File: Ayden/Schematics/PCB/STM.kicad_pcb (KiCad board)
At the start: 2 copper layers, 104.1 x 88.9 mm, 8 parts, among them J1 Screw_Terminal_01x12, U1 NUCLEO-F103RB, U2 NRF24L01_Breakout

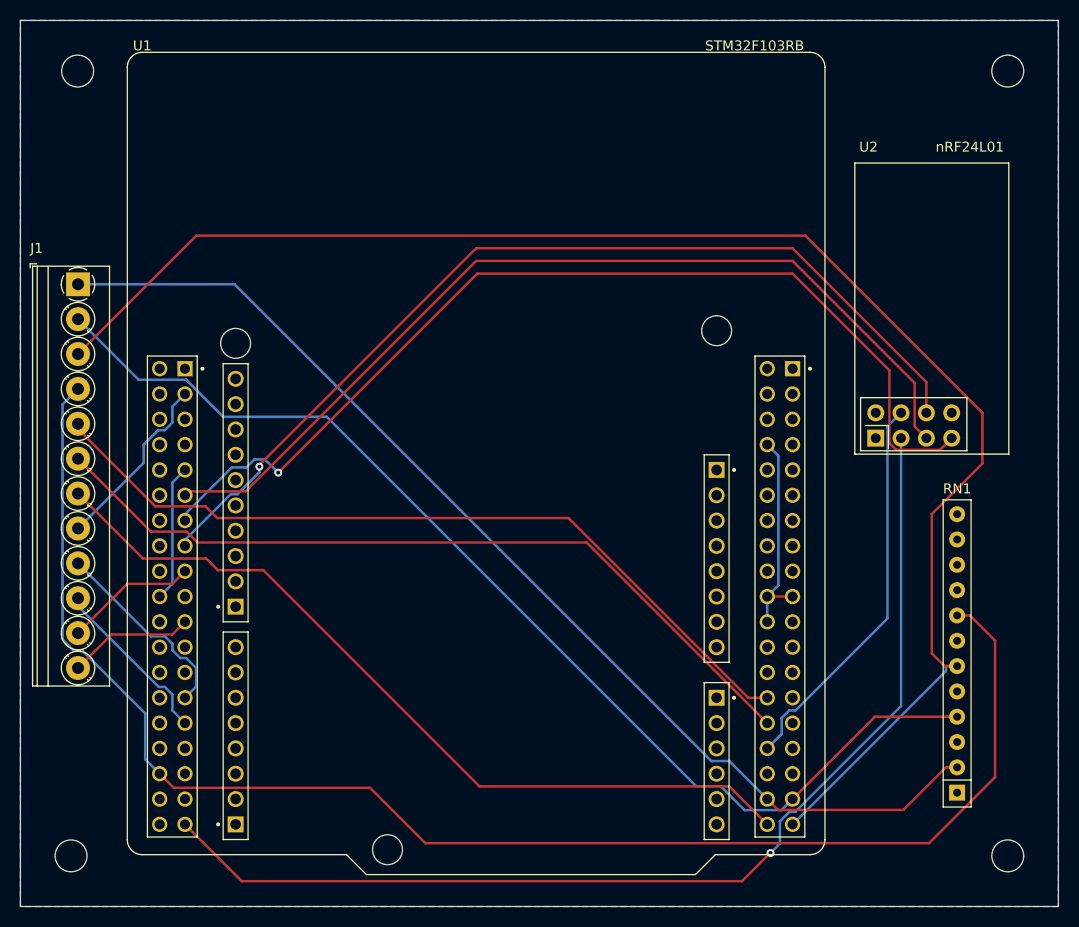
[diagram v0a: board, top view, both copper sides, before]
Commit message: Update schematic/PCB to include connection for common GND
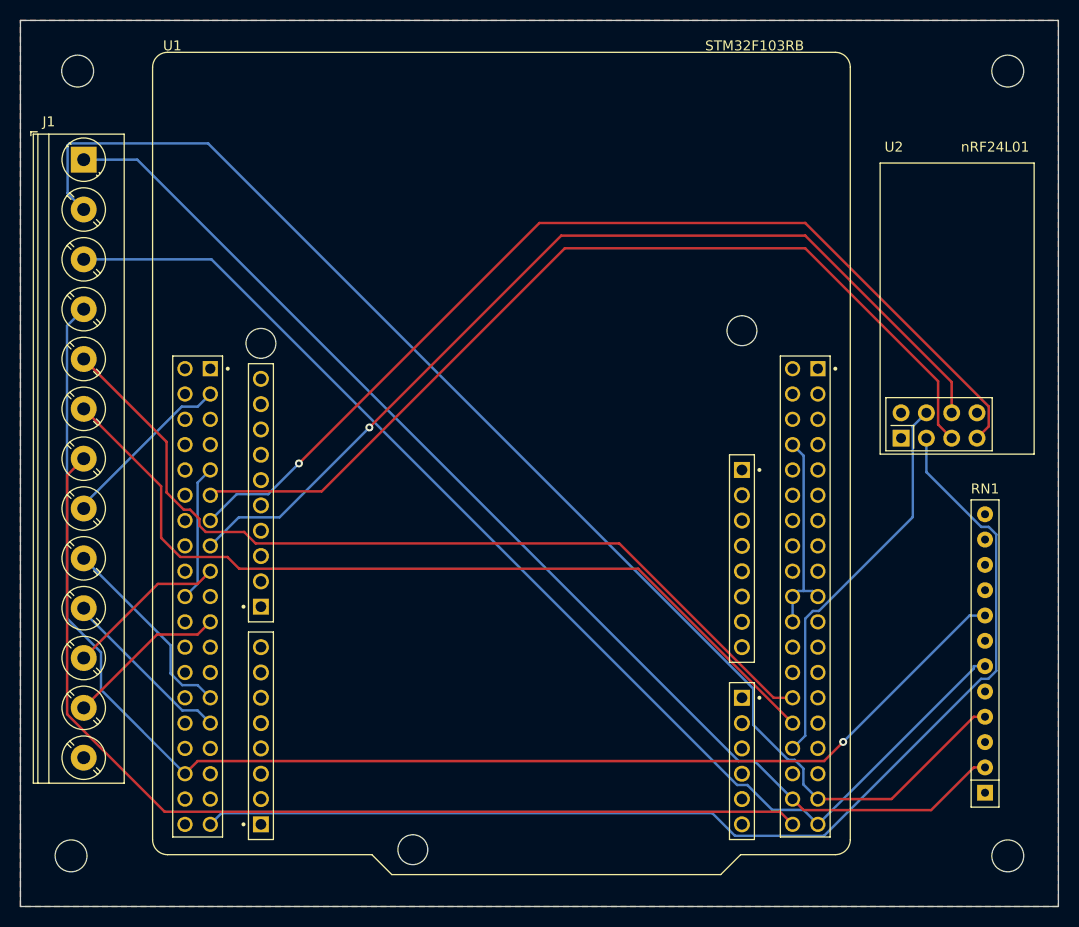
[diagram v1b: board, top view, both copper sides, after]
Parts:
- J1: value Screw_Terminal_01x12 -> Screw_Terminal_01x13; footprint TerminalBlock_Phoenix:TerminalBlock_Phoenix_PT-1,5-12-3.5-H_1x12_P3.50mm_Horizontal -> TerminalBlock_Phoenix:TerminalBlock_Phoenix_PT-1,5-13-5.0-H_1x13_P5.00mm_Horizontal
- moved J1 12.5 mm to (59.7, 69.8)
- moved RN1 2.80 mm to (150.1, 133.4)
- moved U1 2.54 mm to (101.6, 100.3)
- moved U2 2.54 mm to (141.7, 97.8)
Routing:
- net Net-(RN1-Pad6): track 155.7 -> 120.6 mm
- net Net-(U1-PadCN7_38): track 82.9 -> 103.7 mm
- net Net-(RN1-Pad4): track 112.5 -> 133.0 mm
- net Net-(RN1-Pad8): track 151.8 -> 139.1 mm, vias 0 -> 1
- net Net-(U1-PadCN7_28): track 80.8 -> 88.6 mm
- net Net-(RN1-Pad2): track 111.8 -> 119.2 mm
- net Net-(U1-PadCN7_30): track 80.1 -> 87.2 mm
- net Net-(U1-PadCN10_37): track 109.7 -> 113.8 mm, vias 1 -> 0
- net Net-(U1-PadCN10_21): track 12.6 -> 16.3 mm
- net Net-(U1-PadCN10_17): track 13.3 -> 16.3 mm
- net Net-(U1-PadCN10_11): track 94.0 -> 95.1 mm
- net Net-(U1-PadCN10_13): track 100.7 -> 101.8 mm
- net Net-(U1-PadCN10_3): track 18.3 -> 17.7 mm
- net Net-(U1-PadCN7_19): track 21.2 -> 20.7 mm
- added copper zone on F.Cu, net +3.3V
- added copper zone on B.Cu, net GND
- removed copper zone on B.Cu, net +3.3V
- removed copper zone on F.Cu, net GND
